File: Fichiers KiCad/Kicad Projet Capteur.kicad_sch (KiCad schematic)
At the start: 20 parts, among them J1 Power, J2 Digital/PWM, J3 Analog, J4 Digital/PWM, U1 LTC1050#CN8, U2 MCP41050

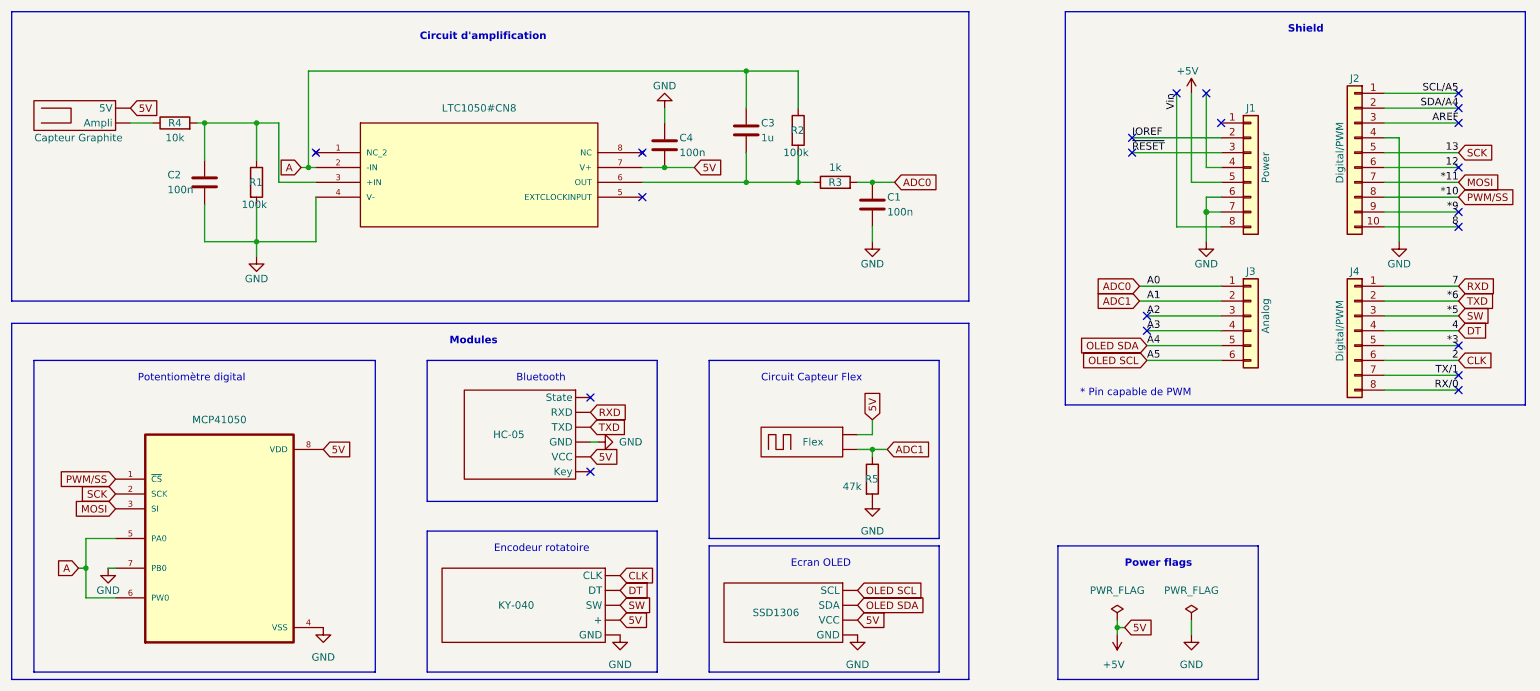
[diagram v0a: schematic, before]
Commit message: Amélioration layout KiCad
OLED +
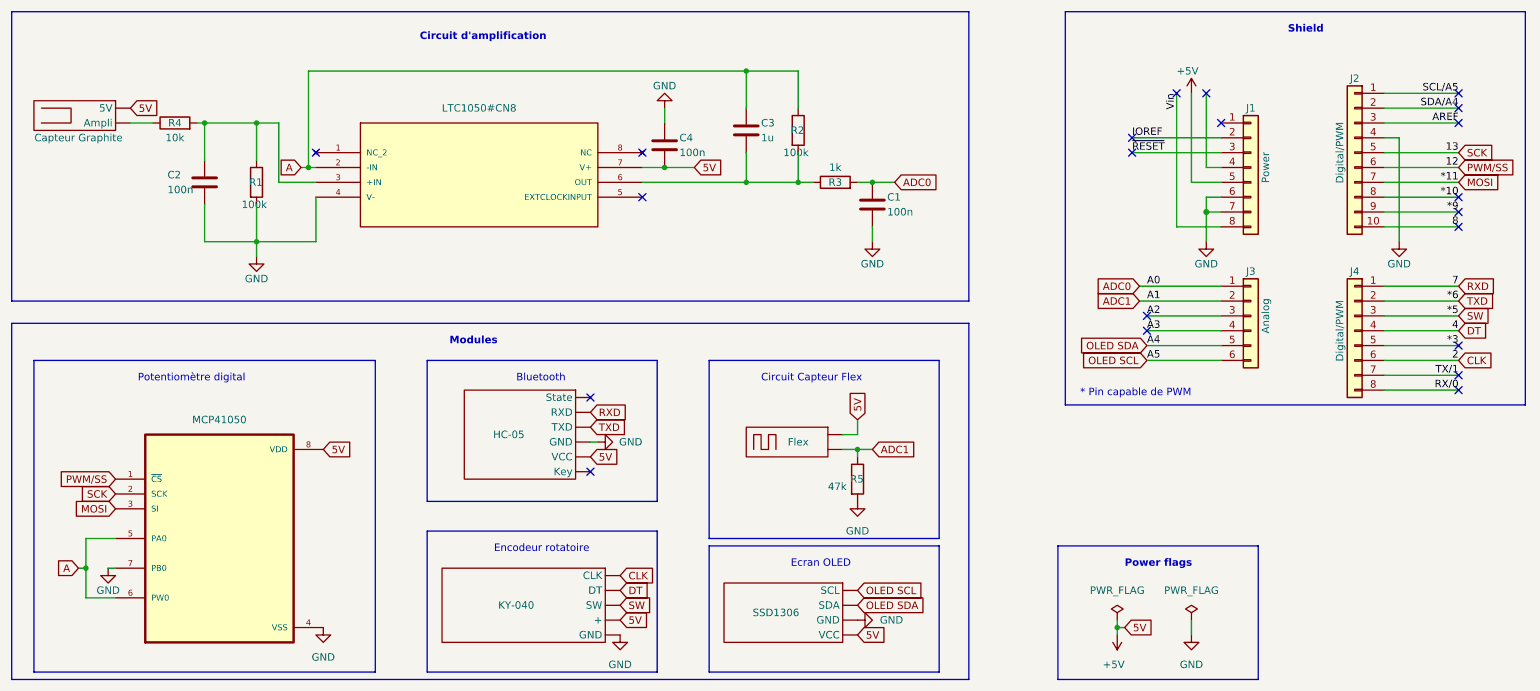
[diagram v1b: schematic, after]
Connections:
- net 12 is gone; now on net PWM/SS: J2.6 (Pin_6)
- net +5V: now also SSD1306.4 (VCC); no longer SSD1306.3 (VCC)
- net GND: now also SSD1306.3 (GND); no longer SSD1306.4 (GND)
- net PWM/SS: no longer J2.8 (Pin_8)
- new net *10: J2.8 (Pin_8)
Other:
- moved on the sheet: R5
